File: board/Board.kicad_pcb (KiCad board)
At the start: 2 copper layers, 58.5 x 58.5 mm, 71 parts, among them J1 GS3, J10 CONN_01X03, J12 GS3, J14 CONN_01X02, J15 CONN_01X07, J16 GS2, J17 CONN_01X01, J2 CONN_02X04, J3 CONN_01X03, J4 CONN_01X03, J5 CONN_01X03, J6 CONN_01X03, J7 CONN_01X03, J8 CONN_01X03, J9 CONN_01X03, SW1 SW_Push, U1 STM32F410RBTx, U2 SN74LVC1G04, U3 LF33ABDT-TR, U4 ICM-20689, U5 MAG3110, U6 MS5637, Y1 25 MHz

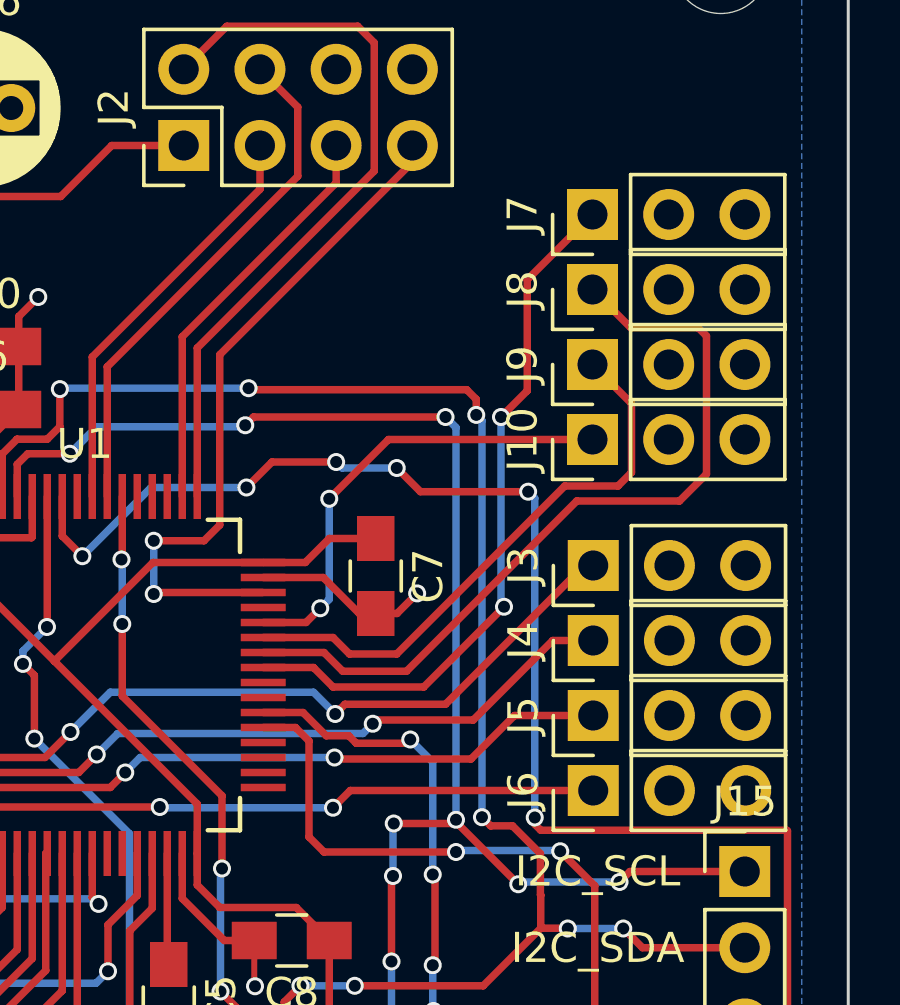
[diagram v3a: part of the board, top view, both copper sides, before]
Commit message: input/output silkscreen
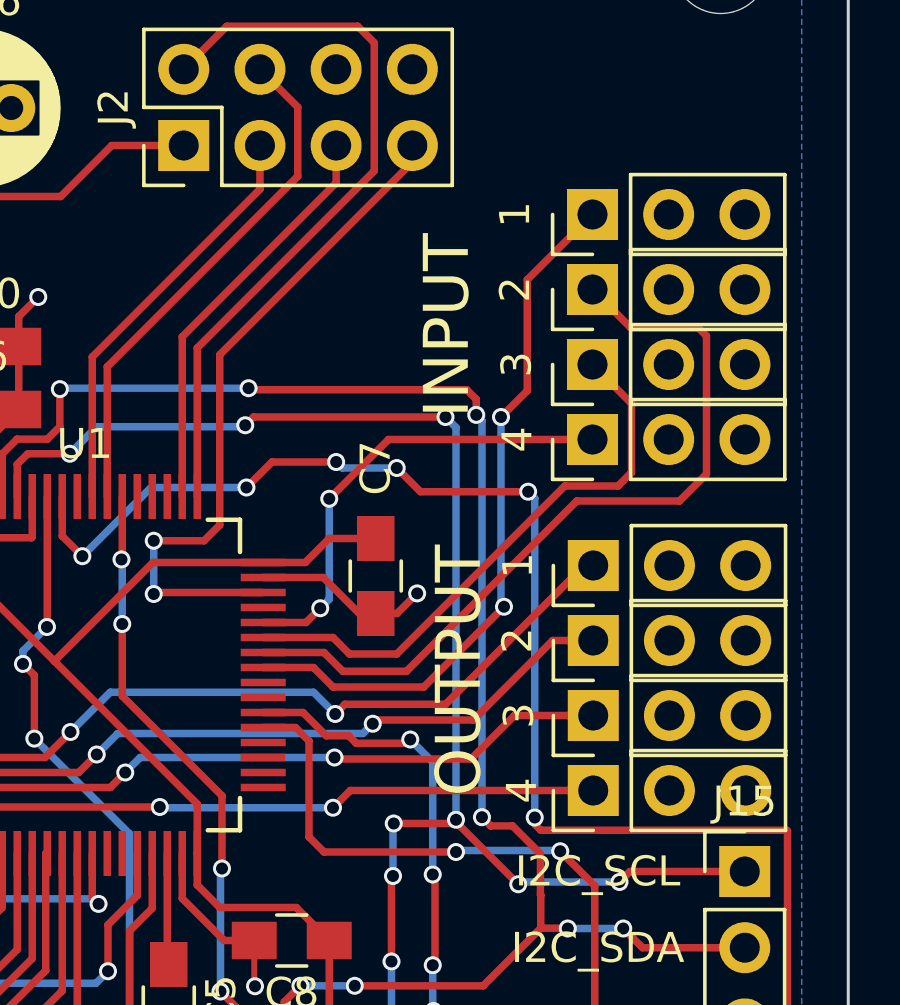
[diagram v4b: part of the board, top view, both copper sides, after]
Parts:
- renumbered J3 to 1, J7 to 1, J4 to 2, J8 to 2, J5 to 3, J9 to 3, J6 to 4, J10 to 4
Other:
- board text added: "INPUT"
- board text added: "OUTPUT"
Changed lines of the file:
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@@
     (links 161)
     (no_connects 5)
-    (area 95.681217 65.689424 154.310576 124.300001)
+    (area 90.442857 64.575 159.557143 125.275)
     (thickness 1.6)
-    (drawings 22)
+    (drawings 24)
     (tracks 766)
     (zones 0)
@@
     (tags "capacitor 0805")
     (attr smd)
-    (fp_text reference C7 (at 0 -1.75 270) (layer F.SilkS)
+    (fp_text reference C7 (at -3.6 0 270) (layer F.SilkS)
       (effects (font (size 1 1) (thickness 0.15)))
     )
@@
       (effects (font (size 1 1) (thickness 0.15)))
     )
-    (fp_text user %R (at 0 -1.75 270) (layer F.Fab)
+    (fp_text user %R (at -3.625 0 270) (layer F.Fab)
       (effects (font (size 1 1) (thickness 0.15)))
     )
@@
     (descr "Through hole straight pin header, 1x03, 2.54mm pitch, single row")
     (tags "Through hole pin header THT 1x03 2.54mm single row")
-    (fp_text reference J3 (at 0 -2.33 90) (layer F.SilkS)
+    (fp_text reference 1 (at 0 -2.5 90) (layer F.SilkS)
       (effects (font (size 1 1) (thickness 0.15)))
     )
@@
     (fp_line (start 1.8 6.85) (end 1.8 -1.8) (layer F.CrtYd) (width 0.05))
     (fp_line (start 1.8 -1.8) (end -1.8 -1.8) (layer F.CrtYd) (width 0.05))
-    (fp_text user %R (at 0 -2.33 90) (layer F.Fab)
-      (effects (font (size 1 1) (thickness 0.15)))
-    )
     (pad 1 thru_hole rect (at 0 0 90) (size 1.7 1.7) (drill 1) (layers *.Cu *.Mask)
       (net 20 PWM_OUTPUT_1))
@@
     (descr "Through hole straight pin header, 1x03, 2.54mm pitch, single row")
     (tags "Through hole pin header THT 1x03 2.54mm single row")
-    (fp_text reference J4 (at 0 -2.33 90) (layer F.SilkS)
+    (fp_text reference 2 (at 0 -2.525 90) (layer F.SilkS)
       (effects (font (size 1 1) (thickness 0.15)))
     )
@@
     (fp_line (start 1.8 6.85) (end 1.8 -1.8) (layer F.CrtYd) (width 0.05))
     (fp_line (start 1.8 -1.8) (end -1.8 -1.8) (layer F.CrtYd) (width 0.05))
-    (fp_text user %R (at 0 -2.33 90) (layer F.Fab)
-      (effects (font (size 1 1) (thickness 0.15)))
-    )
     (pad 1 thru_hole rect (at 0 0 90) (size 1.7 1.7) (drill 1) (layers *.Cu *.Mask)
       (net 22 PWM_OUTPUT_2))
@@
     (descr "Through hole straight pin header, 1x03, 2.54mm pitch, single row")
     (tags "Through hole pin header THT 1x03 2.54mm single row")
-    (fp_text reference J5 (at 0 -2.33 90) (layer F.SilkS)
+    (fp_text reference 3 (at 0 -2.475 90) (layer F.SilkS)
       (effects (font (size 1 1) (thickness 0.15)))
     )
@@
     (fp_line (start 1.8 6.85) (end 1.8 -1.8) (layer F.CrtYd) (width 0.05))
     (fp_line (start 1.8 -1.8) (end -1.8 -1.8) (layer F.CrtYd) (width 0.05))
-    (fp_text user %R (at 0 -2.33 90) (layer F.Fab)
-      (effects (font (size 1 1) (thickness 0.15)))
-    )
     (pad 1 thru_hole rect (at 0 0 90) (size 1.7 1.7) (drill 1) (layers *.Cu *.Mask)
       (net 24 PWM_OUTPUT_3))
@@
     (descr "Through hole straight pin header, 1x03, 2.54mm pitch, single row")
     (tags "Through hole pin header THT 1x03 2.54mm single row")
-    (fp_text reference J6 (at 0 -2.33 90) (layer F.SilkS)
+    (fp_text reference 4 (at 0 -2.375 90) (layer F.SilkS)
       (effects (font (size 1 1) (thickness 0.15)))
     )
@@
     (fp_line (start 1.8 6.85) (end 1.8 -1.8) (layer F.CrtYd) (width 0.05))
     (fp_line (start 1.8 -1.8) (end -1.8 -1.8) (layer F.CrtYd) (width 0.05))
-    (fp_text user %R (at 0 -2.33 90) (layer F.Fab)
-      (effects (font (size 1 1) (thickness 0.15)))
-    )
     (pad 1 thru_hole rect (at 0 0 90) (size 1.7 1.7) (drill 1) (layers *.Cu *.Mask)
       (net 26 PWM_OUTPUT_4))
@@
     (descr "Through hole straight pin header, 1x03, 2.54mm pitch, single row")
     (tags "Through hole pin header THT 1x03 2.54mm single row")
-    (fp_text reference J7 (at 0 -2.33 90) (layer F.SilkS)
+    (fp_text reference 1 (at 0 -2.575 90) (layer F.SilkS)
       (effects (font (size 1 1) (thickness 0.15)))
     )
@@
     (fp_line (start 1.8 6.85) (end 1.8 -1.8) (layer F.CrtYd) (width 0.05))
     (fp_line (start 1.8 -1.8) (end -1.8 -1.8) (layer F.CrtYd) (width 0.05))
-    (fp_text user %R (at 0 -2.33 90) (layer F.Fab)
-      (effects (font (size 1 1) (thickness 0.15)))
-    )
     (pad 1 thru_hole rect (at 0 0 90) (size 1.7 1.7) (drill 1) (layers *.Cu *.Mask)
       (net 28 PWM_INPUT_1))
@@
     (descr "Through hole straight pin header, 1x03, 2.54mm pitch, single row")
     (tags "Through hole pin header THT 1x03 2.54mm single row")
-    (fp_text reference J8 (at 0 -2.33 90) (layer F.SilkS)
+    (fp_text reference 2 (at 0 -2.575 90) (layer F.SilkS)
       (effects (font (size 1 1) (thickness 0.15)))
     )
@@
     (fp_line (start 1.8 6.85) (end 1.8 -1.8) (layer F.CrtYd) (width 0.05))
     (fp_line (start 1.8 -1.8) (end -1.8 -1.8) (layer F.CrtYd) (width 0.05))
-    (fp_text user %R (at 0 -2.33 90) (layer F.Fab)
-      (effects (font (size 1 1) (thickness 0.15)))
-    )
     (pad 1 thru_hole rect (at 0 0 90) (size 1.7 1.7) (drill 1) (layers *.Cu *.Mask)
       (net 30 PWM_INPUT_2))
@@
     (descr "Through hole straight pin header, 1x03, 2.54mm pitch, single row")
     (tags "Through hole pin header THT 1x03 2.54mm single row")
-    (fp_text reference J9 (at 0 -2.33 90) (layer F.SilkS)
+    (fp_text reference 3 (at 0 -2.525 90) (layer F.SilkS)
       (effects (font (size 1 1) (thickness 0.15)))
     )
@@
     (fp_line (start 1.8 6.85) (end 1.8 -1.8) (layer F.CrtYd) (width 0.05))
     (fp_line (start 1.8 -1.8) (end -1.8 -1.8) (layer F.CrtYd) (width 0.05))
-    (fp_text user %R (at 0 -2.33 90) (layer F.Fab)
-      (effects (font (size 1 1) (thickness 0.15)))
-    )
     (pad 1 thru_hole rect (at 0 0 90) (size 1.7 1.7) (drill 1) (layers *.Cu *.Mask)
       (net 32 PWM_INPUT_3))
@@
     (descr "Through hole straight pin header, 1x03, 2.54mm pitch, single row")
     (tags "Through hole pin header THT 1x03 2.54mm single row")
-    (fp_text reference J10 (at 0 -2.33 90) (layer F.SilkS)
+    (fp_text reference 4 (at 0 -2.5 90) (layer F.SilkS)
       (effects (font (size 1 1) (thickness 0.15)))
     )
@@
     (fp_line (start 1.8 6.85) (end 1.8 -1.8) (layer F.CrtYd) (width 0.05))
     (fp_line (start 1.8 -1.8) (end -1.8 -1.8) (layer F.CrtYd) (width 0.05))
-    (fp_text user %R (at 0 -2.33 90) (layer F.Fab)
-      (effects (font (size 1 1) (thickness 0.15)))
-    )
     (pad 1 thru_hole rect (at 0 0 90) (size 1.7 1.7) (drill 1) (layers *.Cu *.Mask)
       (net 34 PWM_INPUT_4))
@@
     )
   )
+  (gr_text OUTPUT (at 141.275 93.5 90) (layer F.SilkS)
+    (effects (font (size 1.5 1.5) (thickness 0.3)))
+  )
+  (gr_text INPUT (at 140.875 82 90) (layer F.SilkS)
+    (effects (font (size 1.5 1.5) (thickness 0.3)))
+  )
   (gr_line (start 145.375 114.8) (end 139.9 114.8) (angle 90) (layer F.SilkS) (width 0.2))

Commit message: silkscreen
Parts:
- renumbered J1 to ?, J12 to ?, J17 to ?, J2 to JTAG
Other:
- board text added: "+"
- board text added: "-"
- board text added: "BOOT0"
- board text added: "BOOT1"
- board text added: "DC 4V-16V"
- board text added: "RESET"
- board text added: "VBAT+"
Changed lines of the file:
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@@
     (links 161)
     (no_connects 5)
-    (area 90.442857 64.575 159.557143 125.275)
+    (area 95.681217 65.689424 154.310576 124.300001)
     (thickness 1.6)
-    (drawings 24)
+    (drawings 35)
     (tracks 766)
     (zones 0)
@@
     (tags "capacitor 0805")
     (attr smd)
-    (fp_text reference C4 (at -0.375 1.625 90) (layer F.SilkS)
+    (fp_text reference C4 (at -0.01 -1.79 90) (layer F.SilkS)
       (effects (font (size 1 1) (thickness 0.15)))
     )
@@
       (effects (font (size 1 1) (thickness 0.15)))
     )
-    (fp_text user %R (at -0.375 1.625 90) (layer F.Fab)
+    (fp_text user %R (at -0.01 -1.78 90) (layer F.Fab)
       (effects (font (size 1 1) (thickness 0.15)))
     )
@@
     (tags "capacitor 0805")
     (attr smd)
-    (fp_text reference C5 (at 0 -1.75 270) (layer F.SilkS)
+    (fp_text reference C5 (at 0.01 1.66 270) (layer F.SilkS)
       (effects (font (size 1 1) (thickness 0.15)))
     )
@@
       (effects (font (size 1 1) (thickness 0.15)))
     )
-    (fp_text user %R (at 0 -1.75 270) (layer F.Fab)
+    (fp_text user %R (at -0.01 1.66 270) (layer F.Fab)
       (effects (font (size 1 1) (thickness 0.15)))
     )
@@
     (tags "capacitor 0805")
     (attr smd)
-    (fp_text reference C6 (at 0 -1.75) (layer F.SilkS)
+    (fp_text reference C6 (at 3.34 0.01) (layer F.SilkS)
       (effects (font (size 1 1) (thickness 0.15)))
     )
@@
       (effects (font (size 1 1) (thickness 0.15)))
     )
-    (fp_text user %R (at 0 -1.75) (layer F.Fab)
+    (fp_text user %R (at 3.34 0.01) (layer F.Fab)
       (effects (font (size 1 1) (thickness 0.15)))
     )
@@
     (tags "capacitor 0805")
     (attr smd)
-    (fp_text reference C9 (at -0.05 1.55 180) (layer F.SilkS)
+    (fp_text reference C9 (at 0.1 -1.775 180) (layer F.SilkS)
       (effects (font (size 1 1) (thickness 0.15)))
     )
@@
       (effects (font (size 1 1) (thickness 0.15)))
     )
-    (fp_text user %R (at -0.05 1.55 180) (layer F.Fab)
+    (fp_text user %R (at 0.1 -1.775 180) (layer F.Fab)
       (effects (font (size 1 1) (thickness 0.15)))
     )
@@
     (tags "capacitor 0805")
     (attr smd)
-    (fp_text reference C11 (at 0 -1.75 90) (layer F.SilkS)
+    (fp_text reference C11 (at -3.75 0 90) (layer F.SilkS)
       (effects (font (size 1 1) (thickness 0.15)))
     )
@@
       (effects (font (size 1 1) (thickness 0.15)))
     )
-    (fp_text user %R (at 0 -1.75 90) (layer F.Fab)
+    (fp_text user %R (at -3.75 0 90) (layer F.Fab)
       (effects (font (size 1 1) (thickness 0.15)))
     )
@@
     (tags "capacitor 0805")
     (attr smd)
-    (fp_text reference C18 (at 0 -1.75 270) (layer F.SilkS)
+    (fp_text reference C18 (at 3.78 0.005 270) (layer F.SilkS)
       (effects (font (size 1 1) (thickness 0.15)))
     )
@@
       (effects (font (size 1 1) (thickness 0.15)))
     )
-    (fp_text user %R (at 0 -1.75 270) (layer F.Fab)
+    (fp_text user %R (at 3.79 0.015 270) (layer F.Fab)
       (effects (font (size 1 1) (thickness 0.15)))
     )
@@
     (tags "capacitor 0805")
     (attr smd)
-    (fp_text reference C22 (at 0 -1.75 90) (layer F.SilkS)
+    (fp_text reference C22 (at 3.745 -0.01 90) (layer F.SilkS)
       (effects (font (size 1 1) (thickness 0.15)))
     )
@@
       (effects (font (size 1 1) (thickness 0.15)))
     )
-    (fp_text user %R (at 0 -1.75 90) (layer F.Fab)
+    (fp_text user %R (at 3.745 -0.01 90) (layer F.Fab)
       (effects (font (size 1 1) (thickness 0.15)))
     )
@@
     (tags "capacitor 0805")
     (attr smd)
-    (fp_text reference C24 (at 0 -1.75 90) (layer F.SilkS)
+    (fp_text reference C24 (at 3.785 -0.035 90) (layer F.SilkS)
       (effects (font (size 1 1) (thickness 0.15)))
     )
@@
       (effects (font (size 1 1) (thickness 0.15)))
     )
-    (fp_text user %R (at 0 -1.75 90) (layer F.Fab)
+    (fp_text user %R (at 3.785 -0.035 90) (layer F.Fab)
       (effects (font (size 1 1) (thickness 0.15)))
     )
@@
     (tags "LED led 0805 SMD smd SMT smt smdled SMDLED smtled SMTLED")
     (attr smd)
-    (fp_text reference D1 (at 0 -1.45) (layer F.SilkS)
+    (fp_text reference D1 (at 3 0.01) (layer F.SilkS)
       (effects (font (size 1 1) (thickness 0.15)))
     )
@@
     (tags "LED led 0805 SMD smd SMT smt smdled SMDLED smtled SMTLED")
     (attr smd)
-    (fp_text reference D2 (at -0.1 -1.85) (layer F.SilkS)
+    (fp_text reference D2 (at 3.1 0.01) (layer F.SilkS)
       (effects (font (size 1 1) (thickness 0.15)))
     )
@@
     (tags "solder bridge")
     (attr smd)
-    (fp_text reference J1 (at -1.7 0 360) (layer F.SilkS)
+    (fp_text reference "" (at -0.77 -3.275 360) (layer F.SilkS)
       (effects (font (size 1 1) (thickness 0.15)))
     )
@@
     (descr "Through hole straight pin header, 2x04, 2.54mm pitch, double rows")
     (tags "Through hole pin header THT 2x04 2.54mm double row")
-    (fp_text reference J2 (at 1.27 -2.33 90) (layer F.SilkS)
+    (fp_text reference JTAG (at 5.18 3.9 180) (layer F.SilkS)
       (effects (font (size 1 1) (thickness 0.15)))
     )
@@
     (fp_line (start 4.35 9.4) (end 4.35 -1.8) (layer F.CrtYd) (width 0.05))
     (fp_line (start 4.35 -1.8) (end -1.8 -1.8) (layer F.CrtYd) (width 0.05))
-    (fp_text user %R (at 1.27 -2.33 90) (layer F.Fab)
+    (fp_text user %R (at 5.19 3.9 180) (layer F.Fab)
       (effects (font (size 1 1) (thickness 0.15)))
     )
@@
     (tags "solder bridge")
     (attr smd)
-    (fp_text reference J12 (at -0.05 -3.8 360) (layer F.SilkS)
+    (fp_text reference "" (at -0.05 -3.8 360) (layer F.SilkS)
       (effects (font (size 1 1) (thickness 0.15)))
     )
@@
     (descr "Through hole straight pin header, 1x01, 2.54mm pitch, single row")
     (tags "Through hole pin header THT 1x01 2.54mm single row")
-    (fp_text reference J17 (at 0 -2.33) (layer F.SilkS)
+    (fp_text reference "" (at 3.05 0) (layer F.SilkS)
       (effects (font (size 1 1) (thickness 0.15)))
     )
@@
     (tags "resistor 0805")
     (attr smd)
-    (fp_text reference R1 (at 0 -1.7 270) (layer F.SilkS)
+    (fp_text reference R1 (at 3.19 0.04 270) (layer F.SilkS)
       (effects (font (size 1 1) (thickness 0.15)))
     )
@@
     (tags "resistor 0805")
     (attr smd)
-    (fp_text reference R3 (at 0 -1.7) (layer F.SilkS)
+    (fp_text reference R3 (at 3.335 0.02) (layer F.SilkS)
       (effects (font (size 1 1) (thickness 0.15)))
     )
@@
     (tags "resistor 0805")
     (attr smd)
-    (fp_text reference R6 (at -3.45 0 180) (layer F.SilkS)
+    (fp_text reference R6 (at -0.01 1.9 180) (layer F.SilkS)
       (effects (font (size 1 1) (thickness 0.15)))
     )
@@
     (tags "resistor 0805")
     (attr smd)
-    (fp_text reference R8 (at 0 -1.7) (layer F.SilkS)
+    (fp_text reference R8 (at 3.49 -0.03) (layer F.SilkS)
       (effects (font (size 1 1) (thickness 0.15)))
     )
@@
     (tags "resistor 0805")
     (attr smd)
-    (fp_text reference R9 (at 0 -1.7 180) (layer F.SilkS)
+    (fp_text reference R9 (at 0.06 -1.74 180) (layer F.SilkS)
       (effects (font (size 1 1) (thickness 0.15)))
     )
@@
     (descr https://www.omron.com/ecb/products/pdf/en-b3f.pdf)
     (tags "tact sw push 6mm")
-    (fp_text reference SW1 (at 9.775 -0.275 180) (layer F.SilkS)
+    (fp_text reference SW1 (at 4.05 -2.32 360) (layer F.SilkS)
       (effects (font (size 1 1) (thickness 0.15)))
     )
@@
     (tags "TO-252 2Lead")
     (attr smd)
-    (fp_text reference U3 (at 6.15 4.55) (layer F.SilkS)
+    (fp_text reference U3 (at 0 4.625) (layer F.SilkS)
       (effects (font (size 1 1) (thickness 0.15)))
     )
@@
     (tags "QFP 0.5")
     (attr smd)
-    (fp_text reference U1 (at 0 -7.7) (layer F.SilkS)
+    (fp_text reference U1 (at 4.25 -7.77) (layer F.SilkS)
       (effects (font (size 1 1) (thickness 0.15)))
     )
@@
     )
   )
+  (gr_text BOOT1 (at 105.46 99.14) (layer F.SilkS)
+    (effects (font (size 1 1) (thickness 0.2)))
+  )
+  (gr_text 0 (at 102.51 97.13) (layer F.SilkS)
+    (effects (font (size 1.5 1.5) (thickness 0.3)))
+  )
+  (gr_text 1 (at 108.65 97.13) (layer F.SilkS)
+    (effects (font (size 1.5 1.5) (thickness 0.3)))
+  )
+  (gr_text 0 (at 103.68 103.3) (layer F.SilkS)
+    (effects (font (size 1.5 1.5) (thickness 0.3)))
+  )
+  (gr_text 1 (at 109.68 103.3) (layer F.SilkS)
+    (effects (font (size 1.5 1.5) (thickness 0.3)))
+  )
+  (gr_text BOOT0 (at 105.75 105.32) (layer F.SilkS)
+    (effects (font (size 1 1) (thickness 0.2)))
+  )
+  (gr_text "DC 4V-16V" (at 111.59 68.66) (layer F.SilkS)
+    (effects (font (size 1.5 1.5) (thickness 0.3)))
+  )
+  (gr_text RESET (at 97.63 110.19 270) (layer F.SilkS)
+    (effects (font (size 1 1) (thickness 0.2)))
+  )
+  (gr_text VBAT+ (at 97.45 86.42 270) (layer F.SilkS)
+    (effects (font (size 1 1) (thickness 0.2)))
+  )
+  (gr_text + (at 97.35 76.08 90) (layer F.SilkS)
+    (effects (font (size 1.5 1.5) (thickness 0.3)))
+  )
+  (gr_text - (at 97.38 78.72 90) (layer F.SilkS)
+    (effects (font (size 1.5 1.5) (thickness 0.3)))
+  )
   (gr_text OUTPUT (at 141.275 93.5 90) (layer F.SilkS)
